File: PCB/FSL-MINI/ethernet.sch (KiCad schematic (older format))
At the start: 41 parts, among them P201 SI-52003-F, P202 PoE, U201 LAN8720A-CP, U202 SI502

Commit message: routing...
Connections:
- net VDD_ETH: now reaches C201.1, C202.1, C203.1, C209.1, C210.1, L201.2, P201.2 (CT), R202.1, R203.1, R204.1, R205.1, U201.1 (VDD2A), U201.19 (VDD1A)
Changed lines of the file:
@@
 Text Label 6800 3600 0    60   ~ 0
 RXN
+Text Label 5400 1500 0    60   ~ 0
+VDD_ETH
 $EndSCHEMATC

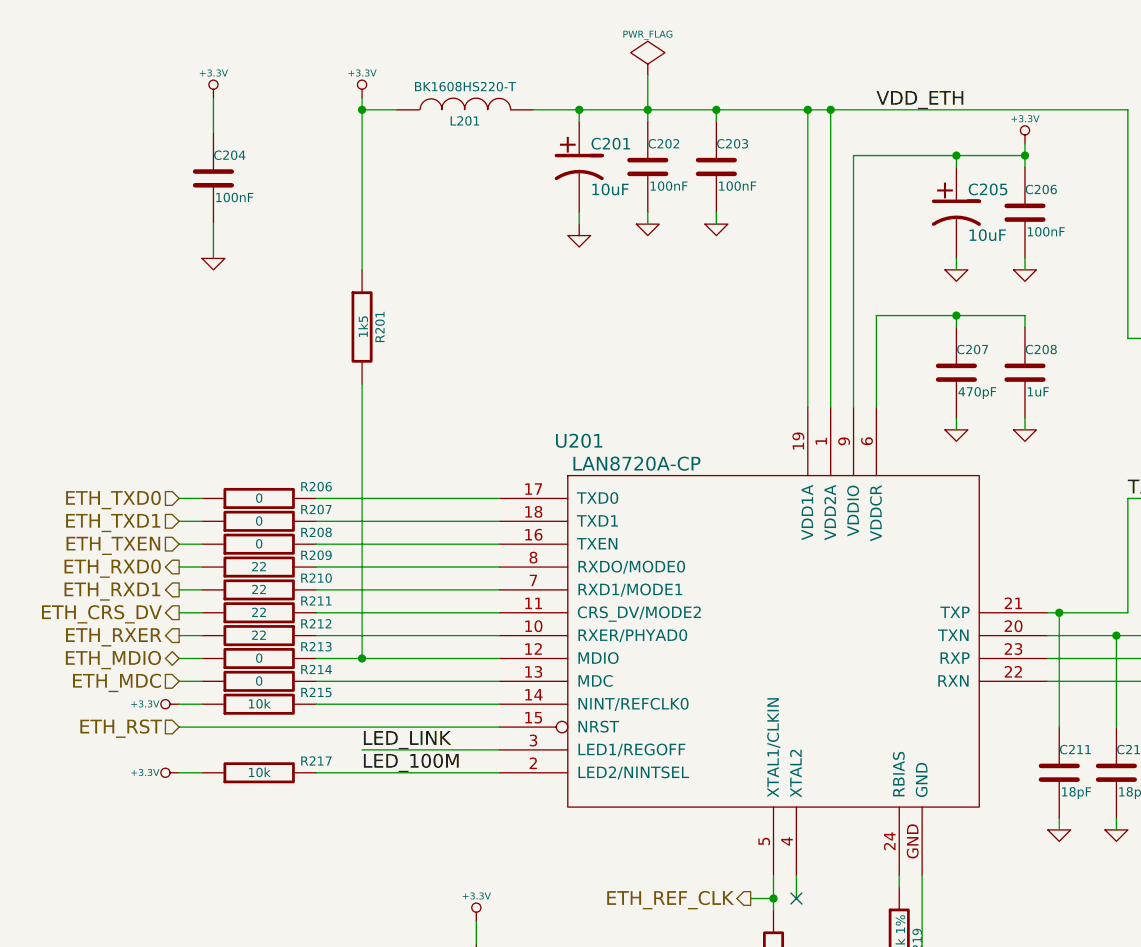
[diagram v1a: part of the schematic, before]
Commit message: Cambio en fuente de pullup de LED2 del phy ethernet según recomendación de hoja de datos.
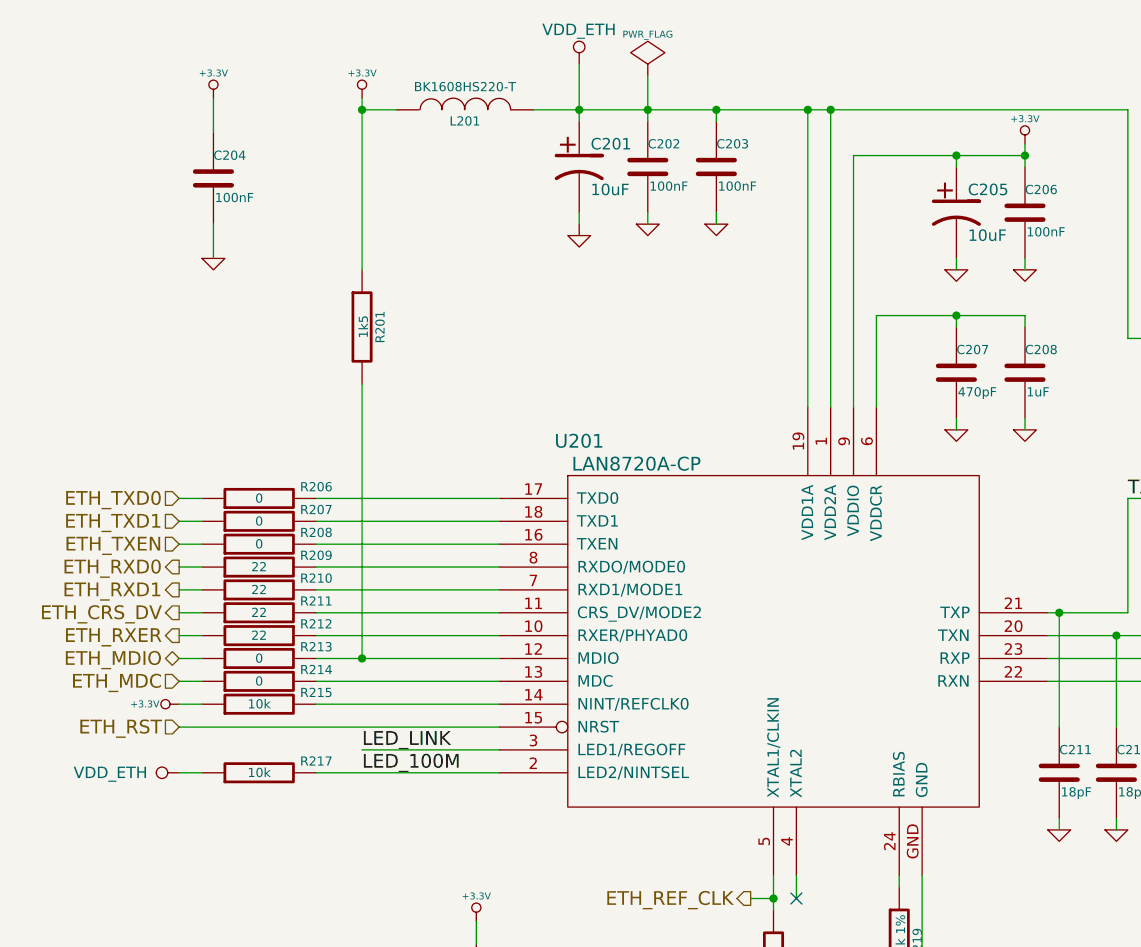
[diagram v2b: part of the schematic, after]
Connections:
- net +3.3V: no longer R217.1
- net VDD_ETH: now also R217.1
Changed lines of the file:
@@
 	4400 1350 4400 1550
 Wire Wire Line
-	4100 1550 4100 1500
+	4100 1300 4100 1550
 Connection ~ 4100 1500
 Wire Wire Line
@@
 	2350 4400 2450 4400
 $Comp
-L +3.3V-RESCUE-ciaa-nxp #PWR024
-U 1 1 52BC2A3B
-P 2350 4400
-F 0 "#PWR024" H 2350 4360 30  0001 C CNN
-F 1 "+3.3V" V 2350 4550 30  0000 C CNN
-F 2 "" H 2350 4400 60  0000 C CNN
-F 3 "" H 2350 4400 60  0000 C CNN
-	1    2350 4400
-	0    -1   -1   0
-$EndComp
-$Comp
 L GND-RESCUE-ciaa-nxp #PWR025
 U 1 1 52BC2B5C
@@
 Text Label 6800 3600 0    60   ~ 0
 RXN
-Text Label 5400 1500 0    60   ~ 0
-VDD_ETH
+$Comp
+L VDD_ETH #PWR?
+U 1 1 57DDACF0
+P 4100 1300
+F 0 "#PWR?" H 4100 1150 50  0001 C CNN
+F 1 "VDD_ETH" H 4100 1450 50  0000 C CNN
+F 2 "" H 4100 1300 50  0000 C CNN
+F 3 "" H 4100 1300 50  0000 C CNN
+	1    4100 1300
+	1    0    0    -1
+$EndComp
+$Comp
+L VDD_ETH #PWR?
+U 1 1 57DDB08B
+P 2350 4400
+F 0 "#PWR?" H 2350 4250 50  0001 C CNN
+F 1 "VDD_ETH" V 2350 4700 50  0000 C CNN
+F 2 "" H 2350 4400 50  0000 C CNN
+F 3 "" H 2350 4400 50  0000 C CNN
+	1    2350 4400
+	0    -1   -1   0
+$EndComp
 $EndSCHEMATC

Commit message: Agregadas notas de aplicación.
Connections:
- net RXN renamed RX_N
- net RXP renamed RX_P
- net TXN renamed TX_N
- net TXP renamed TX_P
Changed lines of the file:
@@
 $EndComp
 Text Label 6500 3200 0    60   ~ 0
-TXP
+TX_P
 Text Label 6600 3400 0    60   ~ 0
-TXN
+TX_N
 Text Label 6700 3500 0    60   ~ 0
-RXP
+RX_P
 Text Label 6800 3600 0    60   ~ 0
-RXN
+RX_N
 $Comp
 L VDD_ETH #PWR?

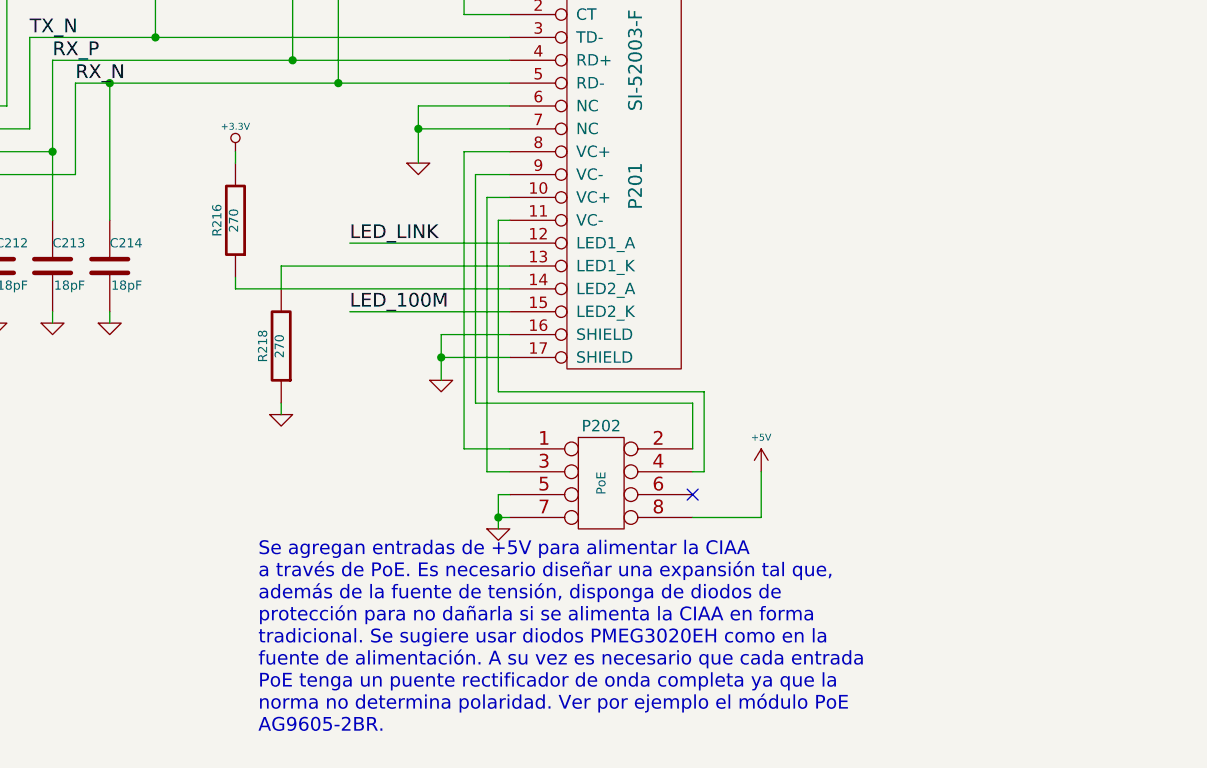
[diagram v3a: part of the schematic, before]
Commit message: Add chassis ground plane attached to both board mounting and RJ45 shield holes.
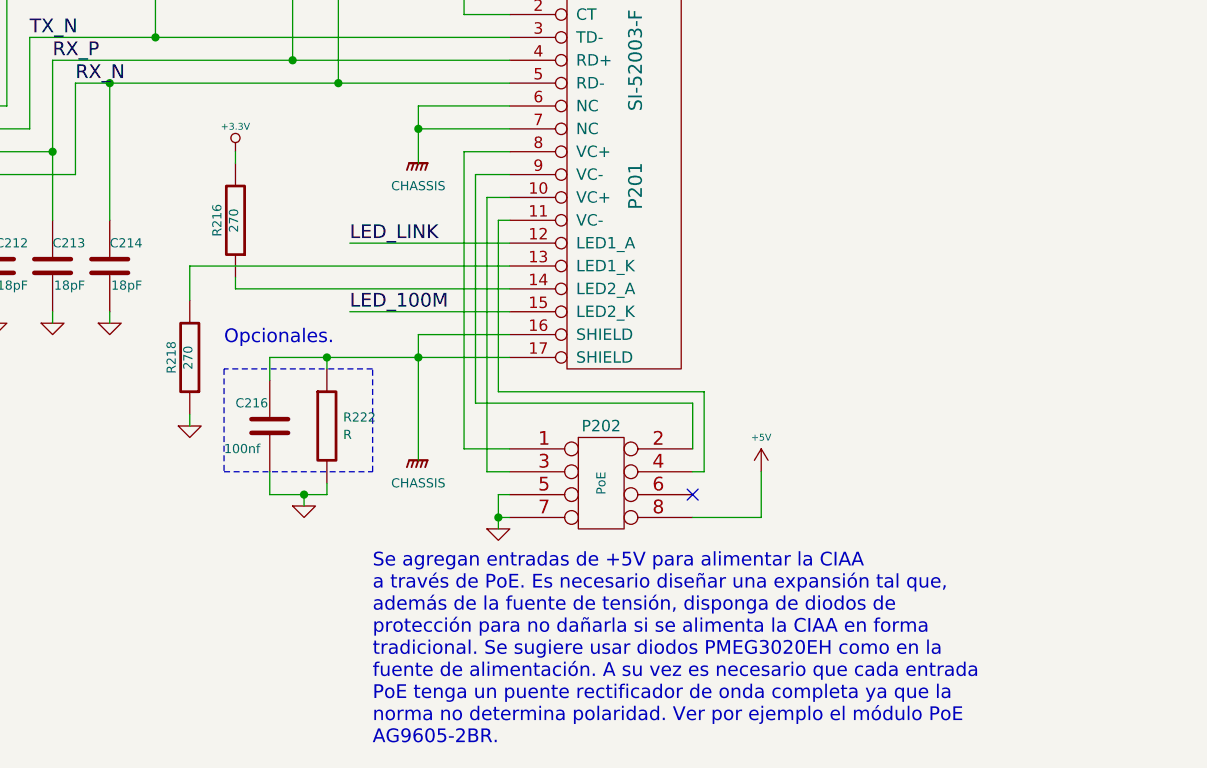
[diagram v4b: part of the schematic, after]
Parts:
- added C216: 100nf, FSL-MINI:c_0603, symbol C
- added R222: R, FSL-MINI:r_0603, symbol R
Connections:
- net GND: now also C216.2, R222.2; no longer P201.16 (SHIELD), P201.17 (SHIELD), P201.6 (NC), P201.7 (NC)
- new net GNDPWR: C216.1, P201.16 (SHIELD), P201.17 (SHIELD), P201.6 (NC), P201.7 (NC), R222.1
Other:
- note added: "Opcionales."
- moved on the sheet: R218
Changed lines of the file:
@@
 L GND-RESCUE-ciaa-nxp #PWR016
 U 1 1 529F7D8C
-P 8400 4900
-F 0 "#PWR016" H 8400 4900 30  0001 C CNN
-F 1 "GND" H 8400 4830 30  0001 C CNN
-F 2 "" H 8400 4900 60  0000 C CNN
-F 3 "" H 8400 4900 60  0000 C CNN
-	1    8400 4900
+P 7800 5450
+F 0 "#PWR016" H 7800 5450 30  0001 C CNN
+F 1 "GND" H 7800 5380 30  0001 C CNN
+F 2 "" H 7800 5450 60  0000 C CNN
+F 3 "" H 7800 5450 60  0000 C CNN
+	1    7800 5450
 	1    0    0    -1
 $EndComp
@@
 L R-RESCUE-ciaa-nxp R218
 U 1 1 529F7EB8
-P 7700 4750
-F 0 "R218" V 7780 4750 40  0000 C CNN
-F 1 "270" V 7707 4751 40  0000 C CNN
-F 2 "FSL-MINI:r_0603" V 7630 4750 30  0001 C CNN
-F 3 "~" H 7700 4750 30  0000 C CNN
-	1    7700 4750
+P 7300 4800
+F 0 "R218" V 7380 4800 40  0000 C CNN
+F 1 "270" V 7307 4801 40  0000 C CNN
+F 2 "FSL-MINI:r_0603" V 7230 4800 30  0001 C CNN
+F 3 "~" H 7300 4800 30  0000 C CNN
+	1    7300 4800
 	-1   0    0    1
 $EndComp
@@
 $EndComp
 Wire Wire Line
-	8700 4400 7700 4400
-Wire Wire Line
-	7700 4400 7700 4500
+	8700 4400 7300 4400
+Wire Wire Line
+	7300 4400 7300 4550
 Wire Wire Line
 	8000 4600 8700 4600
 Wire Wire Line
-	7700 5000 7700 5050
+	7300 5050 7300 5100
 $Comp
 L GND-RESCUE-ciaa-nxp #PWR017
 U 1 1 529F808F
-P 7700 5050
-F 0 "#PWR017" H 7700 5050 30  0001 C CNN
-F 1 "GND" H 7700 4980 30  0001 C CNN
-F 2 "" H 7700 5050 60  0000 C CNN
-F 3 "" H 7700 5050 60  0000 C CNN
-	1    7700 5050
+P 7300 5100
+F 0 "#PWR017" H 7300 5100 30  0001 C CNN
+F 1 "GND" H 7300 5030 30  0001 C CNN
+F 2 "" H 7300 5100 60  0000 C CNN
+F 3 "" H 7300 5100 60  0000 C CNN
+	1    7300 5100
 	1    0    0    -1
 $EndComp
@@
 	2350 4400 2450 4400
 $Comp
-L GND-RESCUE-ciaa-nxp #PWR025
+L GND-RESCUE-ciaa-nxp #PWR024
 U 1 1 52BC2B5C
 P 5200 6200
-F 0 "#PWR025" H 5200 6200 30  0001 C CNN
+F 0 "#PWR024" H 5200 6200 30  0001 C CNN
 F 1 "GND" H 5200 6130 30  0001 C CNN
 F 2 "" H 5200 6200 60  0000 C CNN
@@
 	3650 5150 3650 5050
 $Comp
-L +3.3V-RESCUE-ciaa-nxp #PWR026
+L +3.3V-RESCUE-ciaa-nxp #PWR025
 U 1 1 52BC2DB0
 P 3650 5050
-F 0 "#PWR026" H 3650 5010 30  0001 C CNN
+F 0 "#PWR025" H 3650 5010 30  0001 C CNN
 F 1 "+3.3V" H 3650 5160 30  0000 C CNN
 F 2 "" H 3650 5050 60  0000 C CNN
@@
 	2950 3800 3750 3800
 $Comp
-L +3.3V-RESCUE-ciaa-nxp #PWR027
+L +3.3V-RESCUE-ciaa-nxp #PWR026
 U 1 1 52C68806
 P 7500 3900
-F 0 "#PWR027" H 7500 3860 30  0001 C CNN
+F 0 "#PWR026" H 7500 3860 30  0001 C CNN
 F 1 "+3.3V" H 7500 4010 30  0000 C CNN
 F 2 "" H 7500 3900 60  0000 C CNN
@@
 	8500 3900 8700 3900
 Wire Wire Line
-	8400 4700 8400 4900
-Wire Wire Line
-	8400 4800 8700 4800
-Wire Wire Line
-	8700 4700 8400 4700
-Connection ~ 8400 4800
+	8300 4700 8300 5250
+Wire Wire Line
+	7650 4800 8700 4800
+Wire Wire Line
+	8700 4700 8300 4700
+Connection ~ 8300 4800
 Wire Wire Line
 	7500 4500 8700 4500
 $Comp
-L +5V #PWR028
+L +5V #PWR027
 U 1 1 53F3EF9C
 P 9800 5300
-F 0 "#PWR028" H 9800 5390 20  0001 C CNN
+F 0 "#PWR027" H 9800 5390 20  0001 C CNN
 F 1 "+5V" H 9800 5450 30  0000 C CNN
 F 2 "" H 9800 5300 60  0000 C CNN
@@
 	1    0    0    -1
 $EndComp
-Text Notes 7600 6450 0    60   ~ 0
+Text Notes 8100 6500 0    60   ~ 0
 Se agregan entradas de +5V para alimentar la CIAA\na través de PoE. Es necesario diseñar una expansión tal que, \nademás de la fuente de tensión, disponga de diodos de \nprotección para no dañarla si se alimenta la CIAA en forma \ntradicional. Se sugiere usar diodos PMEG3020EH como en la \nfuente de alimentación. A su vez es necesario que cada entrada\nPoE tenga un puente rectificador de onda completa ya que la \nnorma no determina polaridad. Ver por ejemplo el módulo PoE\nAG9605-2BR.
 $Comp
-L GND-RESCUE-ciaa-nxp #PWR029
+L GND-RESCUE-ciaa-nxp #PWR028
 U 1 1 53F3CD68
 P 8650 5550
-F 0 "#PWR029" H 8650 5550 30  0001 C CNN
+F 0 "#PWR028" H 8650 5550 30  0001 C CNN
 F 1 "GND" H 8650 5480 30  0001 C CNN
 F 2 "" H 8650 5550 60  0000 C CNN
@@
 Wire Wire Line
 	8650 5500 8700 5500
-$Comp
-L GND-RESCUE-ciaa-nxp #PWR030
-U 1 1 5429B31A
-P 8300 3950
-F 0 "#PWR030" H 8300 3950 30  0001 C CNN
-F 1 "GND" H 8300 3880 30  0001 C CNN
-F 2 "" H 8300 3950 60  0000 C CNN
-F 3 "" H 8300 3950 60  0000 C CNN
-	1    8300 3950
-	1    0    0    -1
-$EndComp
 Wire Wire Line
 	8300 3700 8300 3950
@@
 $EndComp
 $Comp
-L PWR_FLAG #FLG031
+L PWR_FLAG #FLG029
 U 1 1 57761D99
 P 4400 1350
-F 0 "#FLG031" H 4400 1445 30  0001 C CNN
+F 0 "#FLG029" H 4400 1445 30  0001 C CNN
 F 1 "PWR_FLAG" H 4400 1530 30  0000 C CNN
 F 2 "" H 4400 1350 60  0000 C CNN
@@
 $EndComp
 $Comp
-L GND-RESCUE-ciaa-nxp #PWR032
+L GND-RESCUE-ciaa-nxp #PWR030
 U 1 1 57763DD1
 P 4700 2000
-F 0 "#PWR032" H 4700 2000 30  0001 C CNN
+F 0 "#PWR030" H 4700 2000 30  0001 C CNN
 F 1 "GND" H 4700 1930 30  0001 C CNN
 F 2 "" H 4700 2000 60  0000 C CNN
@@
 	4700 2000 4700 1950
 $Comp
-L GND-RESCUE-ciaa-nxp #PWR033
+L GND-RESCUE-ciaa-nxp #PWR031
 U 1 1 5774A0EC
 P 4400 2000
-F 0 "#PWR033" H 4400 2000 30  0001 C CNN
+F 0 "#PWR031" H 4400 2000 30  0001 C CNN
 F 1 "GND" H 4400 1930 30  0001 C CNN
 F 2 "" H 4400 2000 60  0000 C CNN
@@
 	4400 2000 4400 1950
 $Comp
-L GND #PWR034
+L GND #PWR032
 U 1 1 5774CEAE
 P 4100 2000
-F 0 "#PWR034" H 4100 2000 30  0001 C CNN
+F 0 "#PWR032" H 4100 2000 30  0001 C CNN
 F 1 "GND" H 4100 1930 30  0001 C CNN
 F 2 "" H 4100 2000 60  0000 C CNN
@@
 RX_N
 $Comp
-L VDD_ETH #PWR?
+L VDD_ETH #PWR033
 U 1 1 57DDACF0
 P 4100 1300
-F 0 "#PWR?" H 4100 1150 50  0001 C CNN
+F 0 "#PWR033" H 4100 1150 50  0001 C CNN
 F 1 "VDD_ETH" H 4100 1450 50  0000 C CNN
 F 2 "" H 4100 1300 50  0000 C CNN
@@
 $EndComp
 $Comp
-L VDD_ETH #PWR?
+L VDD_ETH #PWR034
 U 1 1 57DDB08B
 P 2350 4400
-F 0 "#PWR?" H 2350 4250 50  0001 C CNN
+F 0 "#PWR034" H 2350 4250 50  0001 C CNN
 F 1 "VDD_ETH" V 2350 4700 50  0000 C CNN
 F 2 "" H 2350 4400 50  0000 C CNN
@@
 	0    -1   -1   0
 $EndComp
+$Comp
+L CHASSIS #PWR035
+U 1 1 58241D8B
+P 8300 5250
+F 0 "#PWR035" H 8300 5300 40  0001 C CNN
+F 1 "CHASSIS" H 8300 5150 40  0000 C CNN
+F 2 "" H 8300 5250 60  0000 C CNN
+F 3 "" H 8300 5250 60  0000 C CNN
+	1    8300 5250
+	1    0    0    -1
+$EndComp
+$Comp
+L R R222
+U 1 1 582422B6
+P 7900 5100
+F 0 "R222" H 7971 5138 40  0000 L CNN
+F 1 "R" H 7971 5062 40  0000 L CNN
+F 2 "FSL-MINI:r_0603" V 7830 5100 30  0001 C CNN
+F 3 "" H 7900 5100 30  0000 C CNN
+	1    7900 5100
+	1    0    0    -1
+$EndComp
+$Comp
+L C C216
+U 1 1 58242952
+P 7650 5100
+F 0 "C216" H 7500 5200 40  0000 L CNN
+F 1 "100nf" H 7450 5000 40  0000 L CNN
+F 2 "FSL-MINI:c_0603" H 7688 4950 30  0001 C CNN
+F 3 "" H 7650 5100 60  0000 C CNN
+	1    7650 5100
+	1    0    0    -1
+$EndComp
+Wire Wire Line
+	7650 4800 7650 4900
+Wire Wire Line
+	7900 4850 7900 4800
+Connection ~ 7900 4800
+Wire Wire Line
+	7900 5350 7900 5400
+Wire Wire Line
+	7900 5400 7650 5400
+Wire Wire Line
+	7650 5400 7650 5300
+Wire Wire Line
+	7800 5450 7800 5400
+Connection ~ 7800 5400
+$Comp
+L CHASSIS #PWR036
+U 1 1 582448B8
+P 8300 3950
+F 0 "#PWR036" H 8300 4000 40  0001 C CNN
+F 1 "CHASSIS" H 8300 3850 40  0000 C CNN
+F 2 "" H 8300 3950 60  0000 C CNN
+F 3 "" H 8300 3950 60  0000 C CNN
+	1    8300 3950
+	1    0    0    -1
+$EndComp
+Wire Notes Line
+	7450 4850 7450 5300
+Wire Notes Line
+	7450 5300 8100 5300
+Wire Notes Line
+	8100 5300 8100 4850
+Wire Notes Line
+	8100 4850 7450 4850
+Text Notes 7450 4750 0    60   ~ 0
+Opcionales.
 $EndSCHEMATC

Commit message: Routed USB diferential pair paths.
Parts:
- U202: footprint FSL-MINI:4SMD -> FSL-MINI:Oscillator_7.0x5.0mm
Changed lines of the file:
@@
 F 0 "U202" H 4300 6400 70  0000 C CNN
 F 1 "SI502" H 4300 5400 70  0000 C CNN
-F 2 "FSL-MINI:4SMD" H 4300 5850 60  0001 C CNN
+F 2 "FSL-MINI:Oscillator_7.0x5.0mm" H 4300 5850 60  0001 C CNN
 F 3 "~" H 4300 5850 60  0000 C CNN
 	1    4300 5850
